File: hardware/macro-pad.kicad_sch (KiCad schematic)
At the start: 41 parts

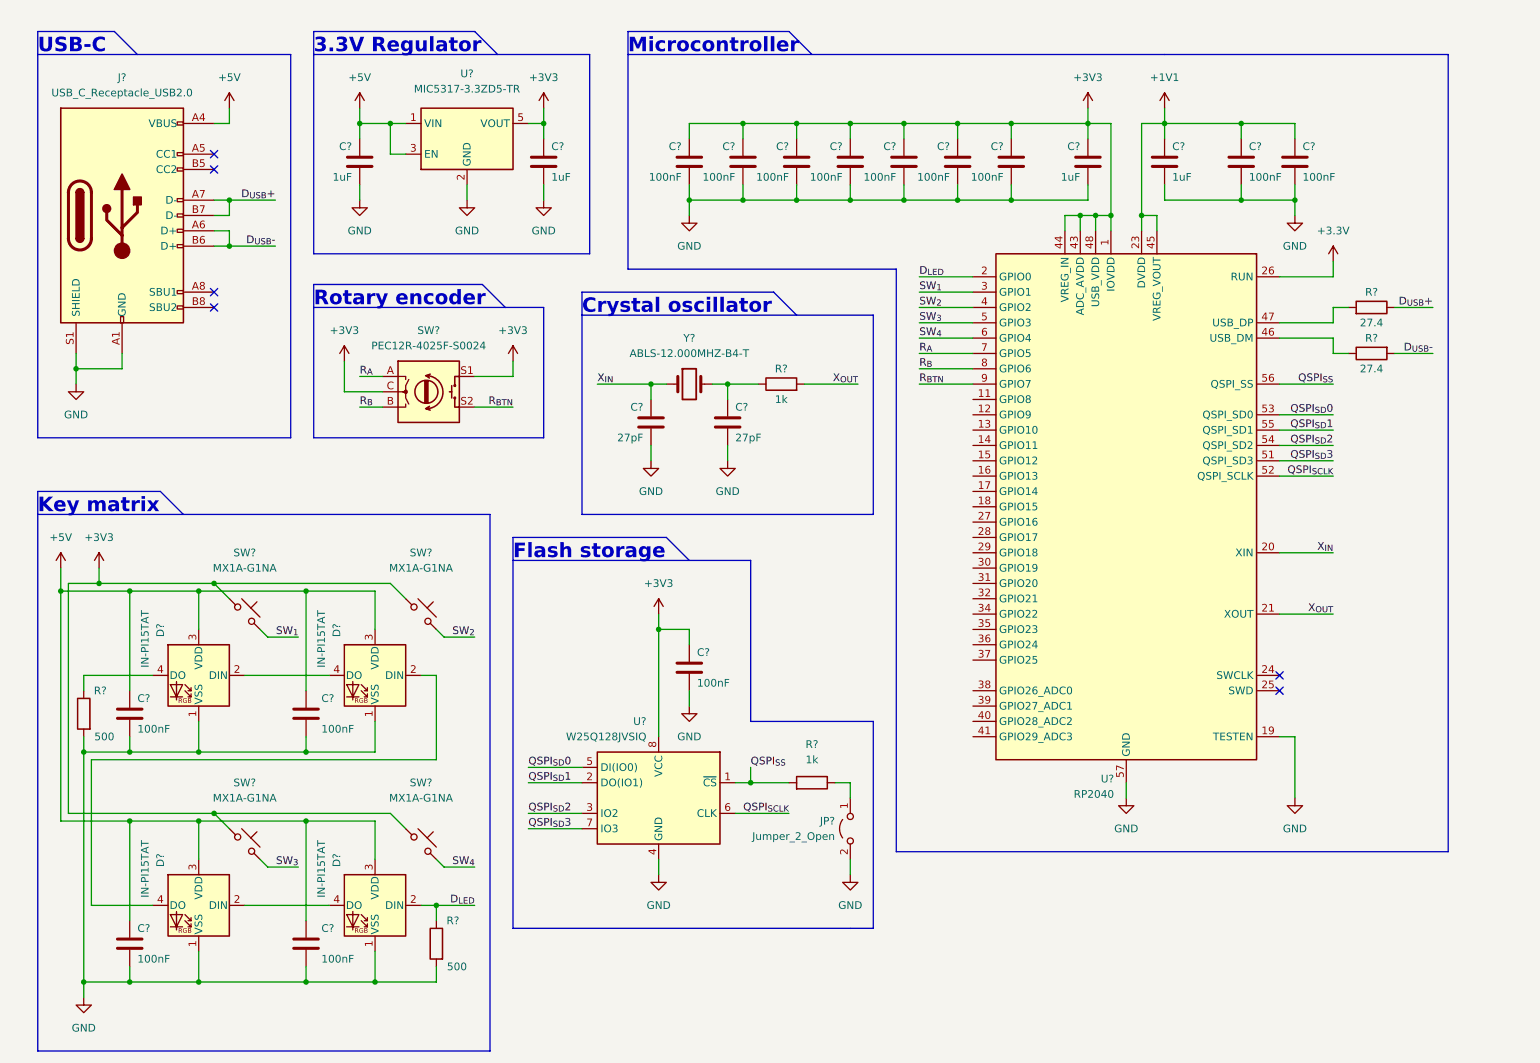
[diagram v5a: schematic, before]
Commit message: Added schematic description
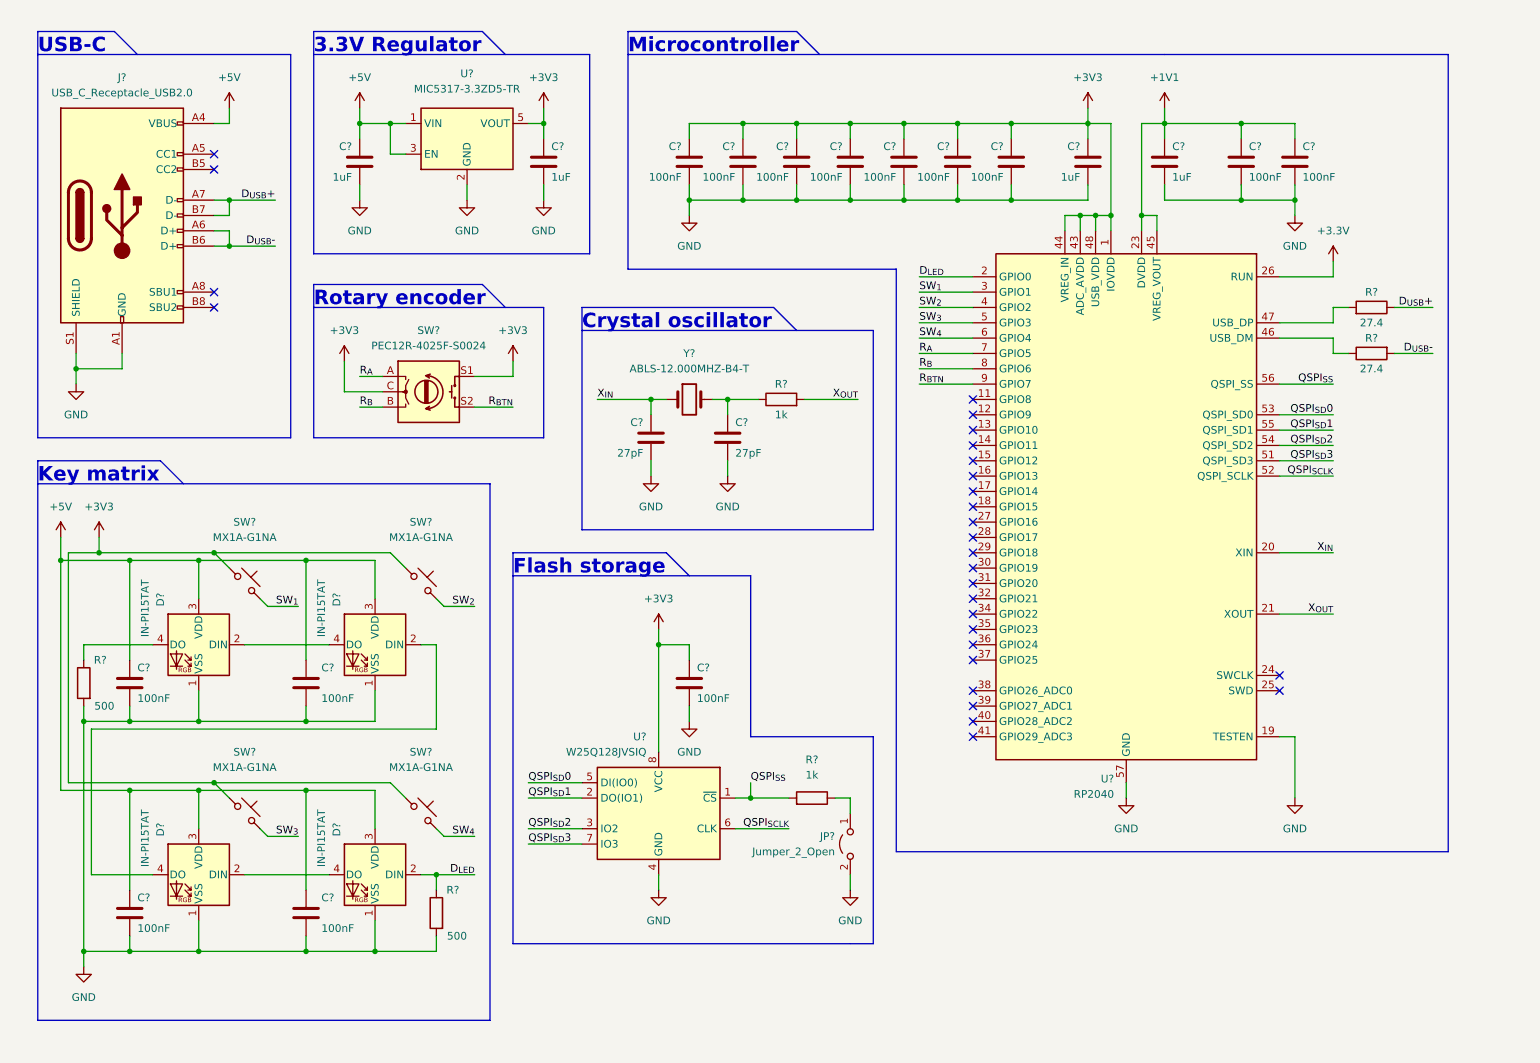
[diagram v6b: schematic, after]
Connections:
- no-connect marks 6 -> 28
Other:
- company: (none) -> EPS@ncl
- title: (none) -> Macro Pad
- moved on the sheet: C?, D?, JP?, R?, SW?, U?, Y?

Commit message: Components have been annotated
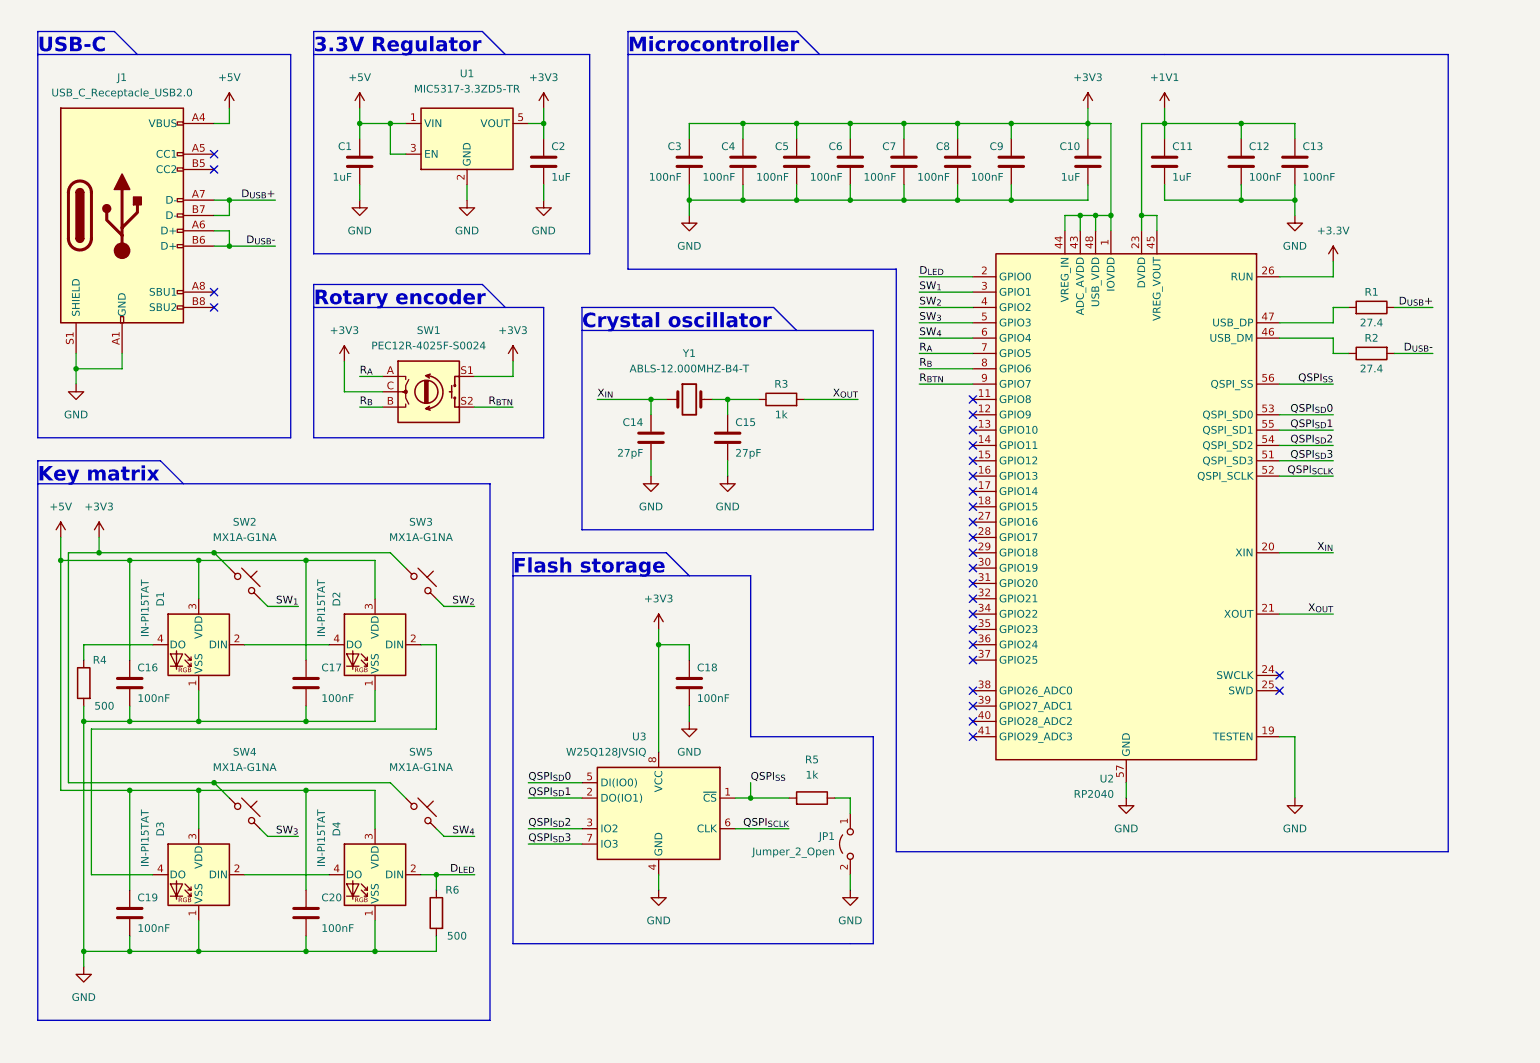
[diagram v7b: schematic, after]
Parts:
- gave numbers to parts that had none: 41

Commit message: All symbols have been associated with a footprint
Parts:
- C1, C10, C11, C12, C13, C14, C15, C16, C17, C18, C19, C2, C20, C3, C4, C5, C6, C7, C8, C9: footprint (none) -> Capacitor_SMD:C_0201_0603Metric_Pad0.64x0.40mm_HandSolder
- J1: footprint (none) -> Connector_USB:USB_C_Receptacle_XKB_U262-16XN-4BVC11
- JP1: footprint (none) -> Connector_PinHeader_2.54mm:PinHeader_1x02_P2.54mm_Vertical
- R1, R2, R3, R4, R5, R6: footprint (none) -> Resistor_SMD:R_0603_1608Metric_Pad0.98x0.95mm_HandSolder
- SW1: footprint (none) -> Rotary_Encoder:RotaryEncoder_Alps_EC11E-Switch_Vertical_H20mm
- SW2, SW3, SW4, SW5: footprint (none) -> Button_Switch_Keyboard:SW_Cherry_MX_1.00u_PCB
- Y1: footprint (none) -> Crystal:Crystal_SMD_HC49-SD_HandSoldering
